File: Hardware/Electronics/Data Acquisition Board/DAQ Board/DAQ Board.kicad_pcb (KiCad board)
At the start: 4 copper layers, 94.7 x 58.9 mm, 157 parts, among them J1 Conn_01x09_Male, J2 USB_B_Mini, J3 Battery Connector, J4 DC Barrel Jack, J5 HC-05 BT Module, J6 ICSP Header, Q1 DMP2100U, SW1 DIP, SW10 SW_SPDT, SW11 SW_SPDT, SW2 SW_DIP_x02, SW3 SW_SPDT, SW4 SW_SPDT, SW5 SW_SPDT, SW6 SW_SPDT, SW7 SW_SPDT, SW8 SW_SPDT, SW9 SW_SPDT, U1 ATmega328P-AU, U2 MCP1755T-5002E_SOT223-5, U3 LM3480-3.3, U4 MCP1755T-5002E_SOT223-5, U5 FT232RL, Y1 16MHz

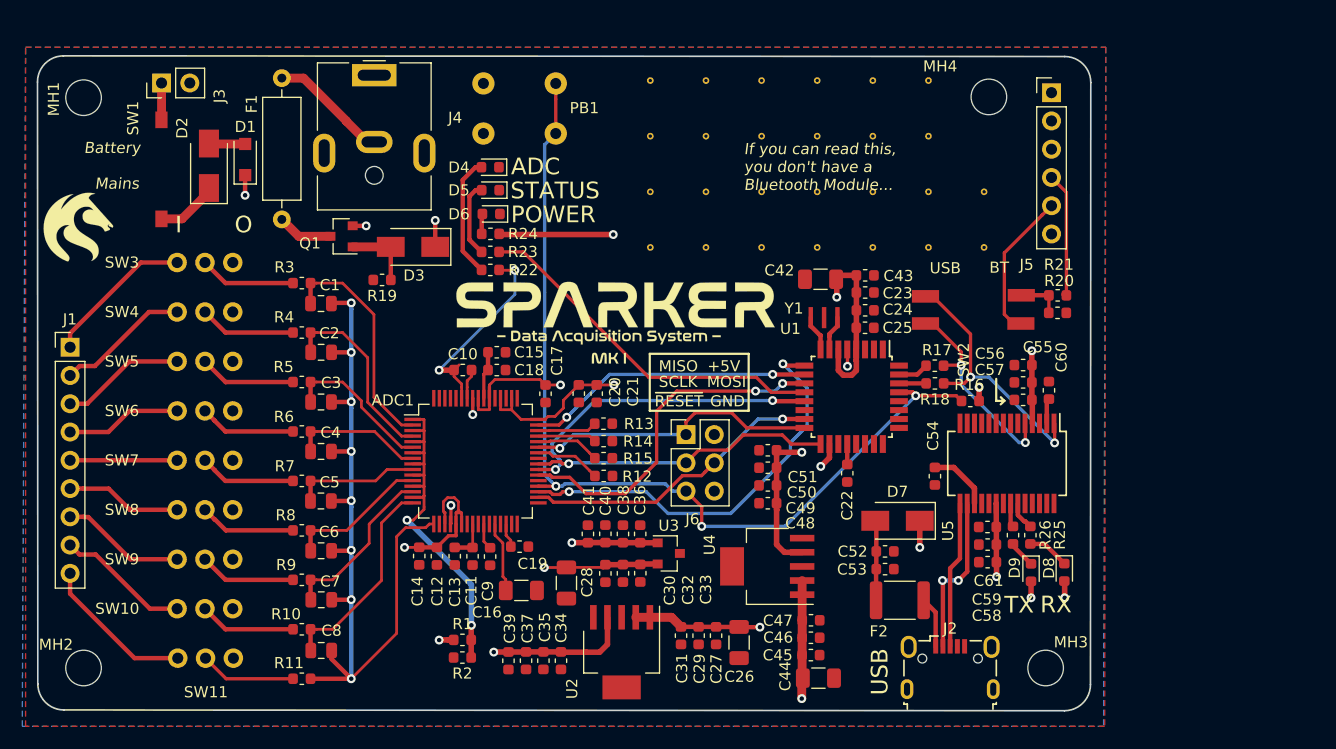
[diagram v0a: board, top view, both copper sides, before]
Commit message: Added test points, initial commit of BoM
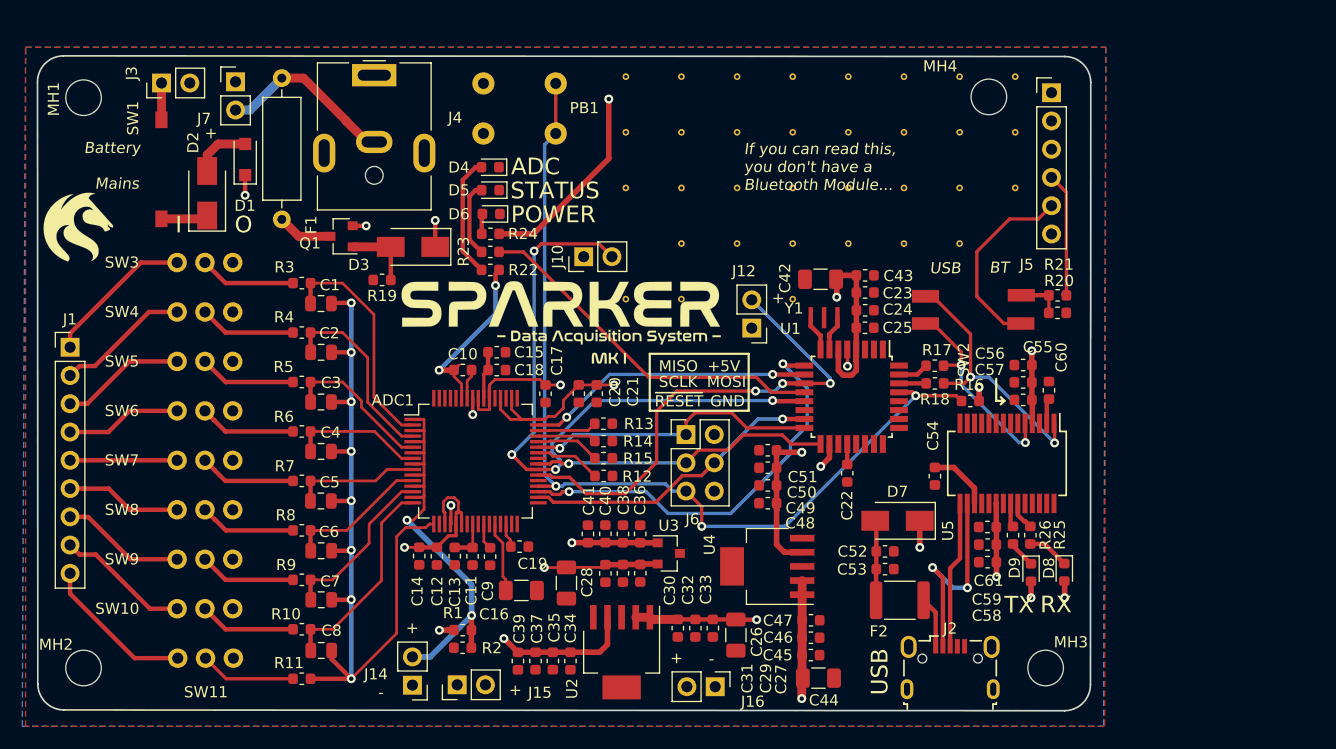
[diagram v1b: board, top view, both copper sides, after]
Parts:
- removed the ? at (203.6, 85.8)
- removed the ? at (193.6, 80.8)
- removed the ? at (188.6, 80.8)
- removed the ? at (183.6, 80.8)
- removed the ? at (178.6, 80.8)
- removed the ? at (173.6, 80.8)
- removed the ? at (198.6, 75.8)
- removed the ? at (193.6, 75.8)
- removed the ? at (188.6, 75.8)
- removed the ? at (183.6, 75.8)
- removed the ? at (178.6, 75.8)
- removed the ? at (198.6, 85.8)
- removed the ? at (173.6, 75.8)
- removed the ? at (198.6, 70.8)
- removed the ? at (193.6, 70.8)
- removed the ? at (188.6, 70.8)
- removed the ? at (183.6, 70.8)
- removed the ? at (178.6, 70.8)
- removed the ? at (173.6, 70.8)
- removed the ? at (193.6, 85.8)
- removed the ? at (188.6, 85.8)
- removed the ? at (183.6, 85.8)
- removed the ? at (178.6, 85.8)
- removed the ? at (173.6, 85.8)
- removed the ? at (203.6, 80.8)
- removed the ? at (198.6, 80.8)
- added ?: , Vias:VIA-0.6mm, F.Cu at (186.4, 90.5)
- added ?: , Vias:VIA-0.6mm, F.Cu at (206.4, 80.5)
- added ?: , Vias:VIA-0.6mm, F.Cu at (201.4, 80.5)
- added ?: , Vias:VIA-0.6mm, F.Cu at (196.4, 80.5)
- added ?: , Vias:VIA-0.6mm, F.Cu at (191.4, 80.5)
- added ?: , Vias:VIA-0.6mm, F.Cu at (186.4, 80.5)
- added ?: , Vias:VIA-0.6mm, F.Cu at (181.4, 80.5)
- added ?: , Vias:VIA-0.6mm, F.Cu at (176.4, 80.5)
- added ?: , Vias:VIA-0.6mm, F.Cu at (171.4, 80.5)
- added ?: , Vias:VIA-0.6mm, F.Cu at (206.4, 75.5)
- added ?: , Vias:VIA-0.6mm, F.Cu at (201.4, 75.5)
- added ?: , Vias:VIA-0.6mm, F.Cu at (176.4, 90.5)
- added ?: , Vias:VIA-0.6mm, F.Cu at (196.4, 75.5)
- added ?: , Vias:VIA-0.6mm, F.Cu at (191.4, 75.5)
- added ?: , Vias:VIA-0.6mm, F.Cu at (186.4, 75.5)
- added ?: , Vias:VIA-0.6mm, F.Cu at (181.4, 75.5)
- added ?: , Vias:VIA-0.6mm, F.Cu at (176.4, 75.5)
- added ?: , Vias:VIA-0.6mm, F.Cu at (171.4, 75.5)
- added ?: , Vias:VIA-0.6mm, F.Cu at (206.4, 70.5)
- added ?: , Vias:VIA-0.6mm, F.Cu at (201.4, 70.5)
- added ?: , Vias:VIA-0.6mm, F.Cu at (196.4, 70.5)
- added ?: , Vias:VIA-0.6mm, F.Cu at (191.4, 70.5)
- added ?: , Vias:VIA-0.6mm, F.Cu at (171.4, 90.5)
- added ?: , Vias:VIA-0.6mm, F.Cu at (186.4, 70.5)
- added ?: , Vias:VIA-0.6mm, F.Cu at (181.4, 70.5)
- added ?: , Vias:VIA-0.6mm, F.Cu at (176.4, 70.5)
- added ?: , Vias:VIA-0.6mm, F.Cu at (171.4, 70.5)
- added ?: , Vias:VIA-0.6mm, F.Cu at (201.4, 85.5)
- added ?: , Vias:VIA-0.6mm, F.Cu at (196.4, 85.5)
- added ?: , Vias:VIA-0.6mm, F.Cu at (191.4, 85.5)
- added ?: , Vias:VIA-0.6mm, F.Cu at (186.4, 85.5)
- added ?: , Vias:VIA-0.6mm, F.Cu at (181.4, 85.5)
- added ?: , Vias:VIA-0.6mm, F.Cu at (176.4, 85.5)
- added J10: ~CS~_TP, Connector_PinHeader_2.54mm:PinHeader_1x02_P2.54mm_Vertical, F.Cu at (167.6, 86.7)
- added J12: START_TP, Connector_PinHeader_2.54mm:PinHeader_1x02_P2.54mm_Vertical, F.Cu at (182.7, 93.1)
- added J14: MID_SUPPLY_TP, Connector_PinHeader_2.54mm:PinHeader_1x02_P2.54mm_Vertical, F.Cu at (152.2, 125.2)
- added J15: AVDD_TP, Connector_PinHeader_2.54mm:PinHeader_1x02_P2.54mm_Vertical, F.Cu at (156.2, 125.1)
- added J16: DVDD_TP, Connector_PinHeader_2.54mm:PinHeader_1x02_P2.54mm_Vertical, F.Cu at (179.4, 125.3)
- added J7: VIN_RAW_TP, Connector_PinHeader_2.54mm:PinHeader_1x02_P2.54mm_Vertical, F.Cu at (136.3, 70.9)
- moved LOGO2 4.92 mm to (165.5, 91.0)
- moved D2 2.48 mm to (133.8, 81.0)
- moved R1 0.88 mm to (156.7, 120.2)
- moved R2 0.88 mm to (156.7, 121.8)
- moved C35 0.85 mm to (164.8, 123.0)
- moved C37 0.85 mm to (163.3, 123.0)
- moved C34 0.85 mm to (166.4, 123.0)
- moved C39 0.85 mm to (161.7, 123.0)
- moved C29 0.73 mm to (177.6, 120.0)
- moved C26 0.73 mm to (181.3, 120.7)
- moved C27 0.73 mm to (179.2, 120.0)
- moved C31 0.73 mm to (176.1, 120.0)
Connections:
- net /ADC1299/START renamed /START
- net /ADC1299/~CS renamed /~CS
- net /ADC1299/~DRDY renamed /~DRDY
- net /ADC1299/~PWDN renamed /~PWDN
- net /ADC1299/~RESET renamed /~RESET
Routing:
- net /~CS: track 28.6 -> 58.5 mm, vias 2 -> 4
- net /ADC1299/DVDD: track 37.8 -> 59.8 mm
- net /START: track 31.4 -> 44.2 mm, vias 2 -> 3
- net /+5V: track 61.8 -> 69.6 mm
- net /ADC1299/MID_SUPPLY: track 33.1 -> 39.1 mm
- net /VIN_RAW: track 10.7 -> 16.1 mm
- net /HC05_TX: track 13.3 -> 18.1 mm
- net Net-(J2-Pad2): track 14.6 -> 18.9 mm
- net /ADC1299/AVDD: track 68.3 -> 65.9 mm
- net /VBAT: track 3.28 -> 5.27 mm
- net Net-(D2-Pad1): track 5.62 -> 4.23 mm
- net /VIN: track 27.8 -> 27.3 mm
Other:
- board text added: "+"
- board text added: "-"

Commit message: Many changes, mostly about rotating the board
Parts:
- removed ? (x33): , Vias:VIA-0.6mm
- removed D1: NSR20F40NXT5GOSCT-ND, Diode_SMD:D_SOD-123F
- removed D2: MURA140T3GOSCT-ND, Diode_SMD:D_SMA
- removed J3: Battery Connector, Connector_PinHeader_2.54mm:PinHeader_1x02_P2.54mm_Vertical
- removed SW1: DIP, Switches:DIP-Switch_01x01
- removed TEXT1: Text, Sparker:NASA_subtext
- moved MH2 108.0 mm to (216.8, 70.8), turned to 180 degrees
- moved MH1 106.5 mm to (216.8, 122.1), turned to 180 degrees
- moved J1 96.7 mm to (218.0, 99.7), turned to 180 degrees
- moved LOGO1 95.4 mm to (212.0, 116.0)
- moved MH3 94.8 mm to (130.4, 70.8), turned to 180 degrees
- moved J5 94.5 mm to (129.8, 122.5), turned to 180 degrees
- moved D8 89.5 mm to (128.7, 79.4), turned to 90 degrees
- moved J7 86.4 mm to (204.9, 123.5), turned to 180 degrees
- moved SW11 84.4 mm to (203.4, 71.7), turned to 0 degrees
- moved D9 84.1 mm to (131.7, 79.4), turned to 90 degrees
- moved R21 82.2 mm to (129.3, 104.3), turned to 0 degrees
- moved R20 81.6 mm to (129.3, 102.8), turned to 180 degrees
- moved R25 81.3 mm to (131.7, 82.8), turned to 270 degrees
- moved J2 81.1 mm to (138.9, 70.9), turned to 180 degrees
- moved SW10 79.5 mm to (203.4, 76.2), turned to 0 degrees
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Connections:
- J5 pad 2: /+5V -> /HC05_TX
- J5 pad 3: /GND -> /HC05_RX
- J5 pad 4: /HC05_RX -> /GND
- J5 pad 5: /HC05_TX -> /+5V
- R21 pad 1: /HC05_RX -> /HC05_TX
- SW2 pad 3: /HC05_TX -> Net-(R20-Pad1)
- SW2 pad 4: Net-(R20-Pad1) -> /HC05_RX
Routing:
- net /~RESET: track 84.5 -> 96.6 mm
- net /VBAT: track 5.27 -> 0.00 mm
- net Net-(D2-Pad1): track 4.23 -> 0.00 mm
- net Net-(J3-Pad1): track 3.31 -> 0.00 mm
- net /HC05_RX: track 11.4 -> 14.4 mm
- net /~CS: track 58.5 -> 60.5 mm
- net /VIN: track 27.3 -> 25.4 mm, vias 5 -> 4
- net /+5V: track 69.6 -> 71.4 mm
- net Net-(R20-Pad1): track 4.05 -> 5.14 mm
- net Net-(D3-Pad2): track 6.39 -> 7.30 mm
- net /HC05_TX: track 18.1 -> 17.4 mm
- net /GND: track 4.68 -> 4.69 mm, vias 3 -> 205
- net Net-(D9-Pad1): vias 0 -> 1
- net (no net): vias 0 -> 1
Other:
- outline, holes or cut-outs redrawn
- board text removed: "Battery"
- board text removed: "Mains"

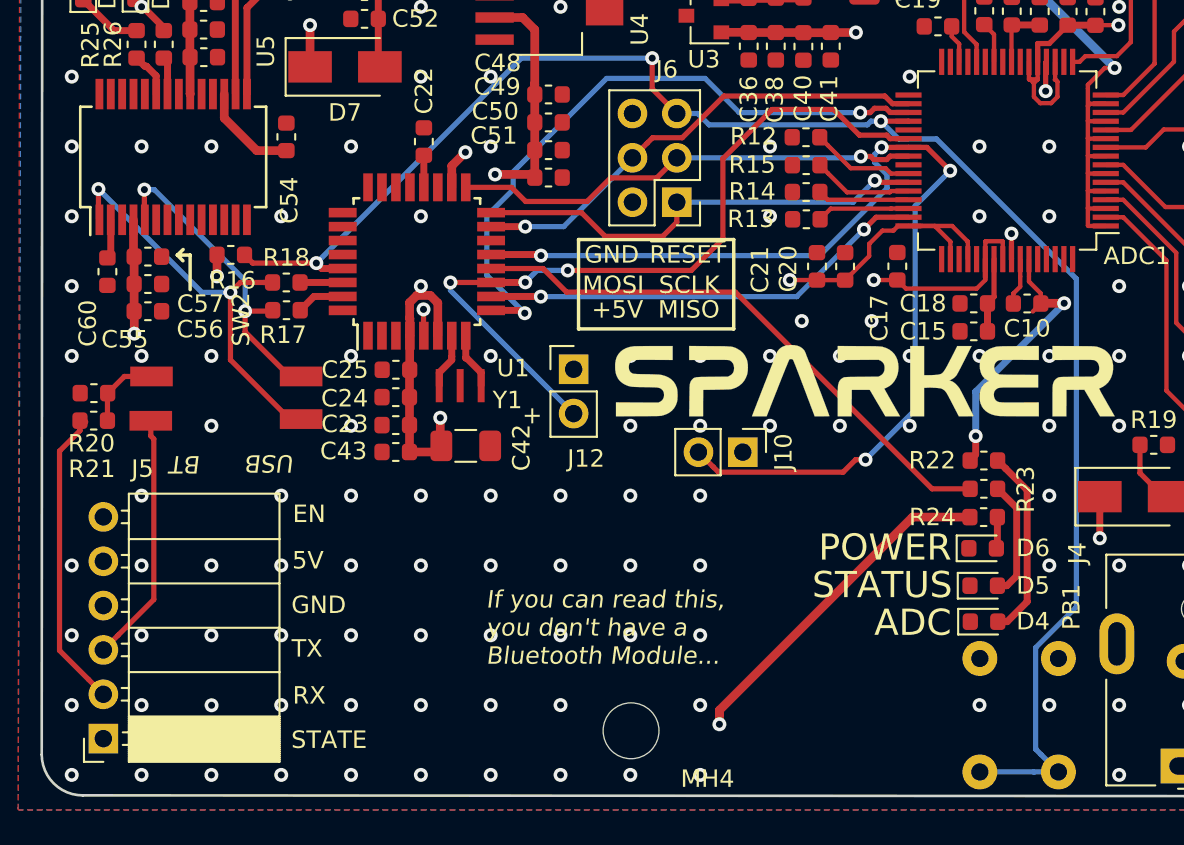
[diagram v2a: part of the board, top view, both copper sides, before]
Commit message: fixed problem where RESET from FTDI chip was connected via cap to GND not RESET. Added 10u cap across reset PB.
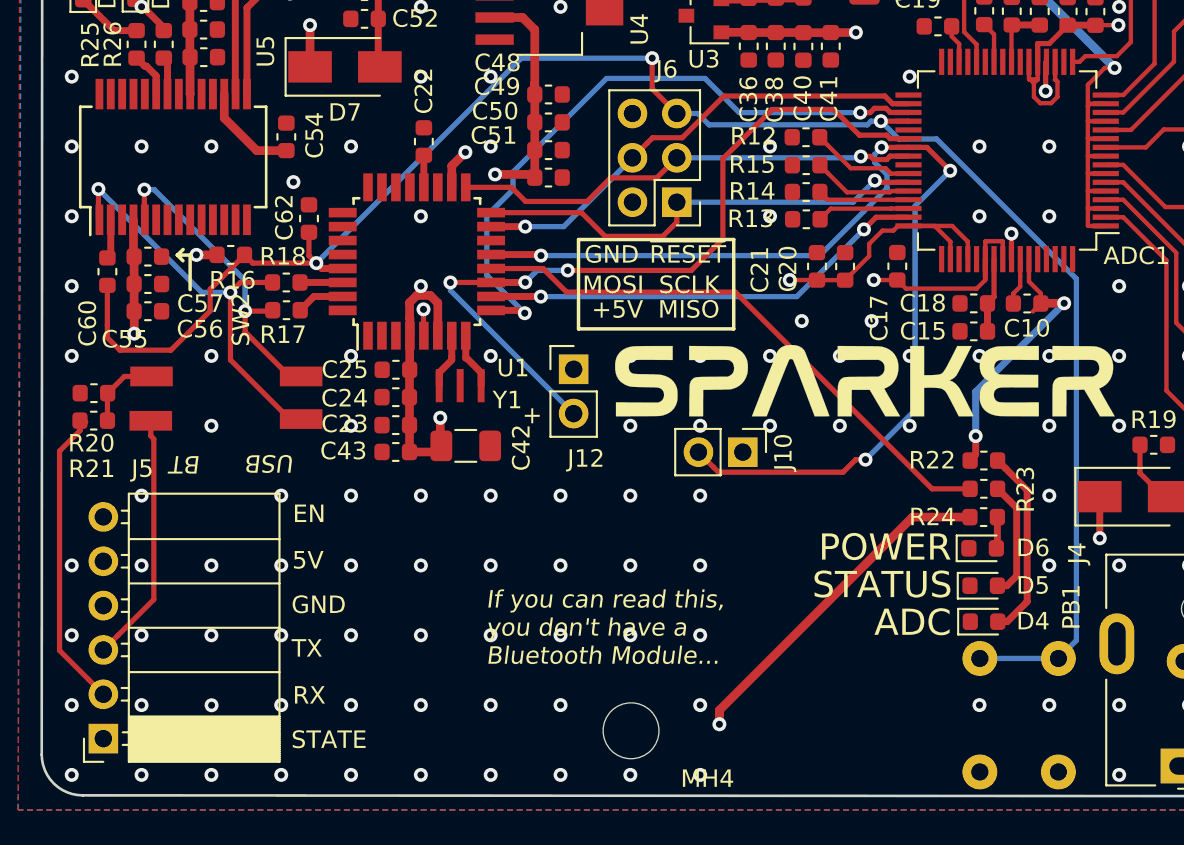
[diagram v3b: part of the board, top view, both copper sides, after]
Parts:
- added C62: 10uF, Capacitor_SMD:C_0603_1608Metric, F.Cu at (141.6, 92.8)
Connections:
- C60 pad 2: /GND -> /~RESET
- PB1 pad 1: /~RESET -> /GND
- PB1 pad 2: /~RESET -> /GND
- PB1 pad 3: /GND -> /~RESET
- PB1 pad 4: /GND -> /~RESET
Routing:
- net /~RESET: track 96.6 -> 105.1 mm
- net /GND: vias 205 -> 204
